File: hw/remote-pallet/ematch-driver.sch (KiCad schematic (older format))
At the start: 7 parts, among them Q2 Q_PMOS_DGS, Q3 Q_NMOS_DGS

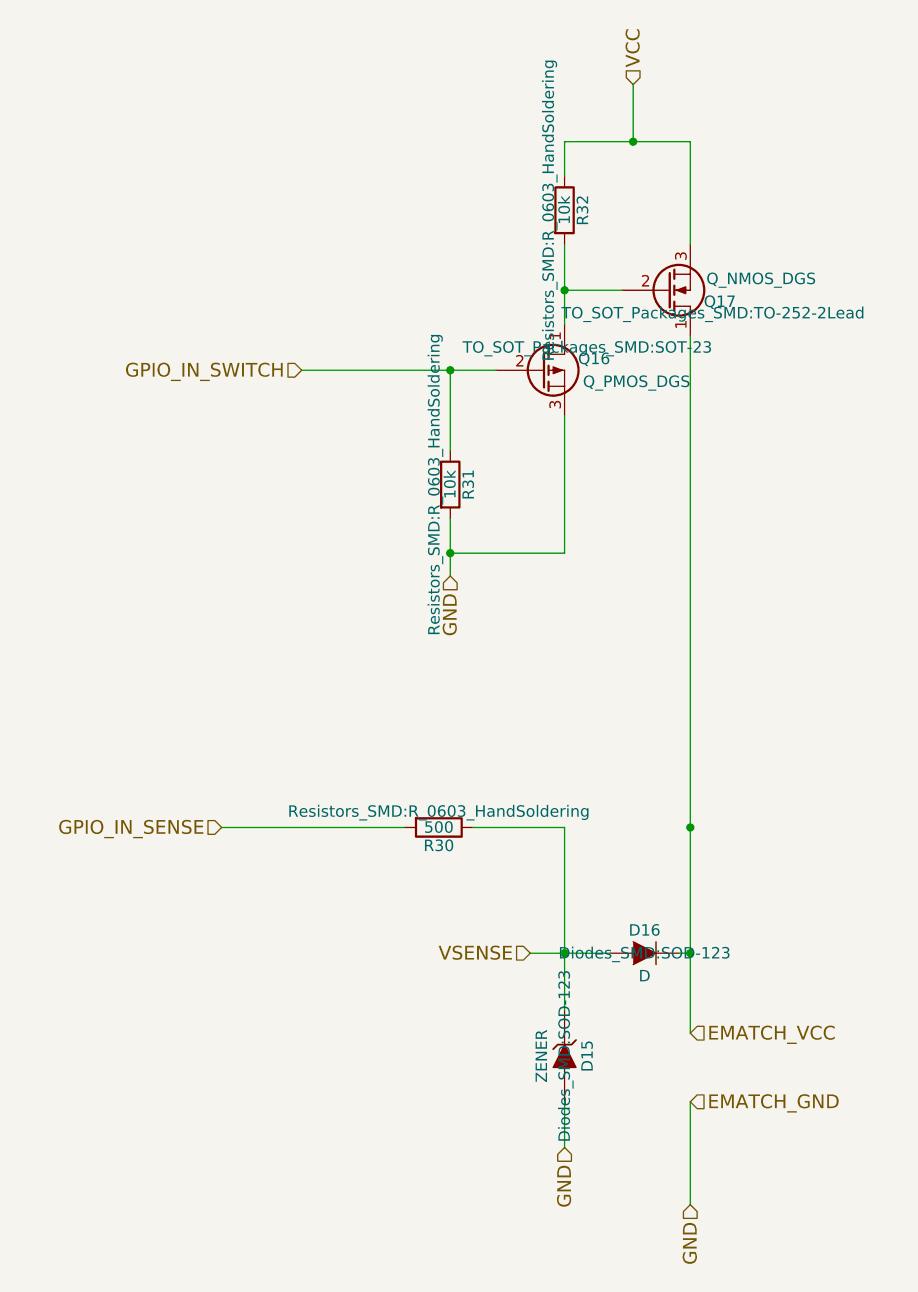
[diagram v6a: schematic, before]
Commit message: updating pcb and adding part numbers for digikey
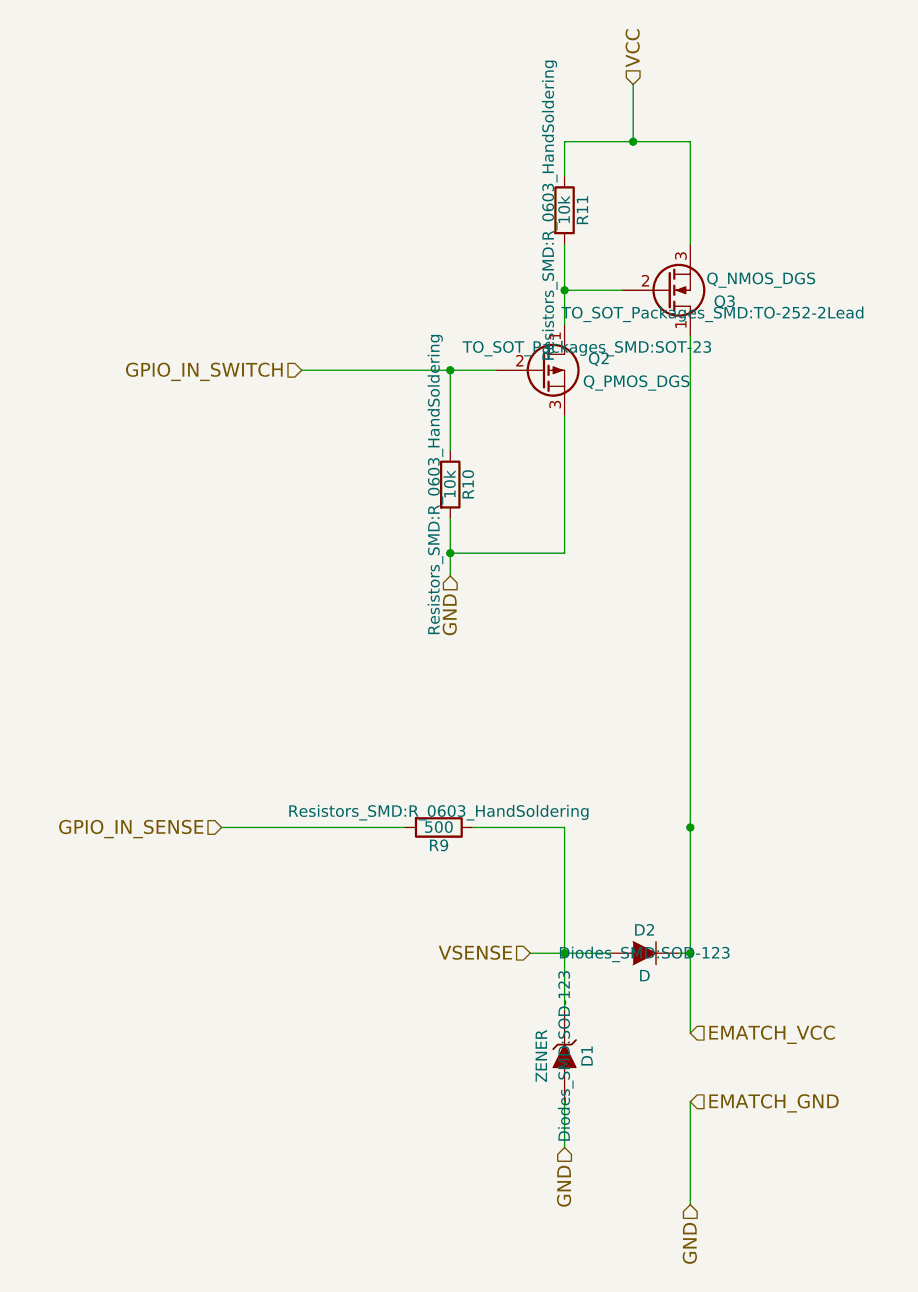
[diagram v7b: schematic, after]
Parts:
- D1: digikey part no (none) -> CD0603-Z3V3CT-ND
- D2: digikey part no (none) -> 641-1282-2-ND
- Q2: digikey part no (none) -> BSS84PH6433XTMA1CT-ND
- Q3: digikey part no (none) -> NTD2955T4GOSCT-ND
- R10, R11: digikey part no (none) -> 311-10KGRCT-ND
- R9: digikey part no (none) -> PLT0603-500ATR-ND
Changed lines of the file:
@@
 AR Path="/56EAA68A/56CFCF8E" Ref="R27"  Part="1"
 AR Path="/56EAA6CF/56CFCF8E" Ref="R30"  Part="1"
-F 0 "R30" V 3080 4100 50  0000 C CNN
+F 0 "R9" V 3080 4100 50  0000 C CNN
 F 1 "500" V 3000 4100 50  0000 C CNN
 F 2 "Resistors_SMD:R_0603_HandSoldering" V 2930 4100 50  0000 C CNN
 F 3 "" H 3000 4100 50  0000 C CNN
+F 4 "PLT0603-500ATR-ND" V 3000 4100 60  0001 C CNN "digikey part no"
 	1    3000 4100
 	0    1    1    0
@@
 AR Path="/56EAA68A/56CFD0B3" Ref="R28"  Part="1"
 AR Path="/56EAA6CF/56CFD0B3" Ref="R31"  Part="1"
-F 0 "R31" V 3130 2600 50  0000 C CNN
+F 0 "R10" V 3130 2600 50  0000 C CNN
 F 1 "10k" V 3050 2600 50  0000 C CNN
 F 2 "Resistors_SMD:R_0603_HandSoldering" V 2980 2600 50  0000 C CNN
 F 3 "" H 3050 2600 50  0000 C CNN
+F 4 "311-10KGRCT-ND" V 3050 2600 60  0001 C CNN "digikey part no"
 	1    3050 2600
 	1    0    0    -1
@@
 AR Path="/56EAA68A/56CFD248" Ref="Q15"  Part="1"
 AR Path="/56EAA6CF/56CFD248" Ref="Q17"  Part="1"
-F 0 "Q17" H 4300 1800 50  0000 R CNN
+F 0 "Q3" H 4300 1800 50  0000 R CNN
 F 1 "Q_NMOS_DGS" H 4650 1700 50  0000 R CNN
 F 2 "TO_SOT_Packages_SMD:TO-252-2Lead" H 4200 1850 50  0000 C CNN
 F 3 "" H 4000 1750 50  0000 C CNN
+F 4 "NTD2955T4GOSCT-ND" H 4000 1750 60  0001 C CNN "digikey part no"
 	1    4000 1750
 	1    0    0    1
@@
 AR Path="/56EAA68A/56CFDBA4" Ref="Q14"  Part="1"
 AR Path="/56EAA6CF/56CFDBA4" Ref="Q16"  Part="1"
-F 0 "Q16" H 3750 2150 50  0000 R CNN
+F 0 "Q2" H 3750 2150 50  0000 R CNN
 F 1 "Q_PMOS_DGS" H 4100 2050 50  0000 R CNN
 F 2 "TO_SOT_Packages_SMD:SOT-23" H 3650 2200 50  0000 C CNN
 F 3 "" H 3450 2100 50  0000 C CNN
+F 4 "BSS84PH6433XTMA1CT-ND" H 3450 2100 60  0001 C CNN "digikey part no"
 	1    3450 2100
 	1    0    0    -1
@@
 AR Path="/56EAA68A/56CFDBE5" Ref="R29"  Part="1"
 AR Path="/56EAA6CF/56CFDBE5" Ref="R32"  Part="1"
-F 0 "R32" V 3630 1400 50  0000 C CNN
+F 0 "R11" V 3630 1400 50  0000 C CNN
 F 1 "10k" V 3550 1400 50  0000 C CNN
 F 2 "Resistors_SMD:R_0603_HandSoldering" V 3480 1400 50  0000 C CNN
 F 3 "" H 3550 1400 50  0000 C CNN
+F 4 "311-10KGRCT-ND" V 3550 1400 60  0001 C CNN "digikey part no"
 	1    3550 1400
 	1    0    0    -1
@@
 AR Path="/56EAA68A/56CFDC9F" Ref="D14"  Part="1"
 AR Path="/56EAA6CF/56CFDC9F" Ref="D16"  Part="1"
-F 0 "D16" H 3900 4750 50  0000 C CNN
+F 0 "D2" H 3900 4750 50  0000 C CNN
 F 1 "D" H 3900 4550 50  0000 C CNN
 F 2 "Diodes_SMD:SOD-123" H 3900 4650 50  0000 C CNN
 F 3 "" H 3900 4650 50  0000 C CNN
+F 4 "641-1282-2-ND" H 3900 4650 60  0001 C CNN "digikey part no"
 	1    3900 4650
 	-1   0    0    -1
@@
 AR Path="/56EAA68A/56CFDD3A" Ref="D13"  Part="1"
 AR Path="/56EAA6CF/56CFDD3A" Ref="D15"  Part="1"
-F 0 "D15" H 3550 5200 50  0000 C CNN
+F 0 "D1" H 3550 5200 50  0000 C CNN
 F 1 "ZENER" H 3550 5000 50  0000 C CNN
 F 2 "Diodes_SMD:SOD-123" H 3550 5100 50  0000 C CNN
 F 3 "" H 3550 5100 50  0000 C CNN
+F 4 "CD0603-Z3V3CT-ND" H 3550 5100 60  0001 C CNN "digikey part no"
 	1    3550 5100
 	0    1    1    0

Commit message: updating schematic and PCB
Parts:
- removed Q3: Q_NMOS_DGS, TO_SOT_Packages_SMD:TO-252-2Lead, symbol Q_NMOS_DGS
- added Q3: Q_NMOS_GDS, TO_SOT_Packages_SMD:TO-252-2Lead, symbol Q_NMOS_GDS
- Q2: symbol Q_PMOS_DGS -> Q_PMOS_GSD
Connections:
- net EMATCH_GND: now also Q2.2 (S); no longer Q2.3 (S)
- net EMATCH_VCC: now also Q3.2 (D)
- net GPIO_IN_SWITCH: now also Q2.1 (G); no longer Q2.2 (G)
- net VCC: now also Q3.3 (S)
- net at R11.2: now also Q2.3 (D), Q3.1 (G); no longer Q2.1 (D)
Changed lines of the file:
@@
 AR Path="/56EAA68A/56CFCF8E" Ref="R27"  Part="1"
 AR Path="/56EAA6CF/56CFCF8E" Ref="R30"  Part="1"
-F 0 "R9" V 3080 4100 50  0000 C CNN
+F 0 "R30" V 3080 4100 50  0000 C CNN
 F 1 "500" V 3000 4100 50  0000 C CNN
-F 2 "Resistors_SMD:R_0603_HandSoldering" V 2930 4100 50  0000 C CNN
+F 2 "Resistors_SMD:R_0603_HandSoldering" V 2930 4100 50  0001 C CNN
 F 3 "" H 3000 4100 50  0000 C CNN
 F 4 "PLT0603-500ATR-ND" V 3000 4100 60  0001 C CNN "digikey part no"
@@
 AR Path="/56EAA68A/56CFD0B3" Ref="R28"  Part="1"
 AR Path="/56EAA6CF/56CFD0B3" Ref="R31"  Part="1"
-F 0 "R10" V 3130 2600 50  0000 C CNN
+F 0 "R31" V 3130 2600 50  0000 C CNN
 F 1 "10k" V 3050 2600 50  0000 C CNN
-F 2 "Resistors_SMD:R_0603_HandSoldering" V 2980 2600 50  0000 C CNN
+F 2 "Resistors_SMD:R_0603_HandSoldering" V 2980 2600 50  0001 C CNN
 F 3 "" H 3050 2600 50  0000 C CNN
 F 4 "311-10KGRCT-ND" V 3050 2600 60  0001 C CNN "digikey part no"
@@
 $EndComp
 $Comp
-L Q_NMOS_DGS Q3
-U 1 1 56CFD248
-P 4000 1750
-AR Path="/56CFDAEF/56CFD248" Ref="Q3"  Part="1"
-AR Path="/56D0EADF/56CFD248" Ref="Q5"  Part="1"
-AR Path="/56D11458/56CFD248" Ref="Q7"  Part="1"
-AR Path="/56EA4F7F/56CFD248" Ref="Q9"  Part="1"
-AR Path="/56EAA678/56CFD248" Ref="Q11"  Part="1"
-AR Path="/56EAA681/56CFD248" Ref="Q13"  Part="1"
-AR Path="/56EAA68A/56CFD248" Ref="Q15"  Part="1"
-AR Path="/56EAA6CF/56CFD248" Ref="Q17"  Part="1"
-F 0 "Q3" H 4300 1800 50  0000 R CNN
-F 1 "Q_NMOS_DGS" H 4650 1700 50  0000 R CNN
-F 2 "TO_SOT_Packages_SMD:TO-252-2Lead" H 4200 1850 50  0000 C CNN
-F 3 "" H 4000 1750 50  0000 C CNN
-F 4 "NTD2955T4GOSCT-ND" H 4000 1750 60  0001 C CNN "digikey part no"
-	1    4000 1750
-	1    0    0    1
-$EndComp
-$Comp
-L Q_PMOS_DGS Q2
+L Q_PMOS_GSD Q2
 U 1 1 56CFDBA4
 P 3450 2100
@@
 AR Path="/56EAA68A/56CFDBA4" Ref="Q14"  Part="1"
 AR Path="/56EAA6CF/56CFDBA4" Ref="Q16"  Part="1"
-F 0 "Q2" H 3750 2150 50  0000 R CNN
+F 0 "Q16" H 3750 2150 50  0000 R CNN
 F 1 "Q_PMOS_DGS" H 4100 2050 50  0000 R CNN
-F 2 "TO_SOT_Packages_SMD:SOT-23" H 3650 2200 50  0000 C CNN
-F 3 "" H 3450 2100 50  0000 C CNN
+F 2 "TO_SOT_Packages_SMD:SOT-23" H 3650 2200 50  0001 C CNN
+F 3 "https://www.infineon.com/dgdl/Infineon-BSS84P-DS-v02_07-en.pdf?fileId=db3a304330f68606013118ac7a9b4549" H 3450 2100 50  0001 C CNN
 F 4 "BSS84PH6433XTMA1CT-ND" H 3450 2100 60  0001 C CNN "digikey part no"
 	1    3450 2100
@@
 AR Path="/56EAA68A/56CFDBE5" Ref="R29"  Part="1"
 AR Path="/56EAA6CF/56CFDBE5" Ref="R32"  Part="1"
-F 0 "R11" V 3630 1400 50  0000 C CNN
+F 0 "R32" V 3630 1400 50  0000 C CNN
 F 1 "10k" V 3550 1400 50  0000 C CNN
-F 2 "Resistors_SMD:R_0603_HandSoldering" V 3480 1400 50  0000 C CNN
+F 2 "Resistors_SMD:R_0603_HandSoldering" V 3480 1400 50  0001 C CNN
 F 3 "" H 3550 1400 50  0000 C CNN
 F 4 "311-10KGRCT-ND" V 3550 1400 60  0001 C CNN "digikey part no"
@@
 AR Path="/56EAA68A/56CFDC9F" Ref="D14"  Part="1"
 AR Path="/56EAA6CF/56CFDC9F" Ref="D16"  Part="1"
-F 0 "D2" H 3900 4750 50  0000 C CNN
+F 0 "D16" H 3900 4750 50  0000 C CNN
 F 1 "D" H 3900 4550 50  0000 C CNN
-F 2 "Diodes_SMD:SOD-123" H 3900 4650 50  0000 C CNN
+F 2 "Diodes_SMD:SOD-123" H 3900 4650 50  0001 C CNN
 F 3 "" H 3900 4650 50  0000 C CNN
 F 4 "641-1282-2-ND" H 3900 4650 60  0001 C CNN "digikey part no"
@@
 AR Path="/56EAA68A/56CFDD3A" Ref="D13"  Part="1"
 AR Path="/56EAA6CF/56CFDD3A" Ref="D15"  Part="1"
-F 0 "D1" H 3550 5200 50  0000 C CNN
+F 0 "D15" H 3550 5200 50  0000 C CNN
 F 1 "ZENER" H 3550 5000 50  0000 C CNN
-F 2 "Diodes_SMD:SOD-123" H 3550 5100 50  0000 C CNN
+F 2 "Diodes_SMD:SOD-123" H 3550 5100 50  0001 C CNN
 F 3 "" H 3550 5100 50  0000 C CNN
 F 4 "CD0603-Z3V3CT-ND" H 3550 5100 60  0001 C CNN "digikey part no"
@@
 Wire Wire Line
 	3400 4650 3750 4650
+$Comp
+L Q_NMOS_GDS Q3
+U 1 1 571CE2E9
+P 4000 1750
+AR Path="/56CFDAEF/571CE2E9" Ref="Q3"  Part="1"
+AR Path="/56EAA6CF/571CE2E9" Ref="Q17"  Part="1"
+AR Path="/56D0EADF/571CE2E9" Ref="Q5"  Part="1"
+AR Path="/56D11458/571CE2E9" Ref="Q7"  Part="1"
+AR Path="/56EA4F7F/571CE2E9" Ref="Q9"  Part="1"
+AR Path="/56EAA678/571CE2E9" Ref="Q11"  Part="1"
+AR Path="/56EAA681/571CE2E9" Ref="Q13"  Part="1"
+AR Path="/56EAA68A/571CE2E9" Ref="Q15"  Part="1"
+F 0 "Q17" H 4300 1800 50  0000 R CNN
+F 1 "Q_NMOS_GDS" H 4650 1700 50  0000 R CNN
+F 2 "TO_SOT_Packages_SMD:TO-252-2Lead" H 4200 1850 50  0001 C CNN
+F 3 "http://www.diodes.com/_files/datasheets/DMN10H170SK3.pdf" H 4000 1750 50  0001 C CNN
+F 4 "DMN10H170SK3-13DICT-ND	" H 4000 1750 60  0001 C CNN "digikey part no"
+	1    4000 1750
+	1    0    0    1
+$EndComp
 $EndSCHEMATC
